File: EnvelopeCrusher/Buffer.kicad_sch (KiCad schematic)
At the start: 6 parts, among them U1 TL072

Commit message: Add routing
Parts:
- added C?: ~, symbol Device:C
- C? (x4): value 100nF -> ~; footprint Capacitor_SMD:C_0805_2012Metric_Pad1.18x1.45mm_HandSolder -> (none)
- R?: value 22M -> ~
- U1: value TL072 -> ~
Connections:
- net GND: now also C?.2
- net OUT: now also U1.6 (-), U1.7; no longer U1.1, U1.2 (-)
- net CRUSH_Z: now reaches U1.5 (+)
- net IN renamed DIRECT_OUT
- new net CRUSH_Y: U1.1, U1.2 (-)
- no-connect marks 3 -> 0
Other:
- note added: "74HC4066 Analog Switch"
- moved on the sheet: C?, R?, U1A, U1B

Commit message: updated
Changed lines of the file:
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@@
       (effects (font (size 1.27 1.27)) hide)
     )
-    (property "Value" "" (id 1) (at 130.81 125.0879 0))
+    (property "Value" "-5V" (id 1) (at 130.81 125.0879 0))
     (property "Footprint" "" (id 2) (at 130.81 130.1679 0)
       (effects (font (size 1.27 1.27)) hide)
@@
       (effects (font (size 1.27 1.27)) hide)
     )
-    (property "Value" "" (id 1) (at 143.51 161.29 0))
+    (property "Value" "GND" (id 1) (at 143.51 161.29 0))
     (property "Footprint" "" (id 2) (at 143.51 156.21 0)
       (effects (font (size 1.27 1.27)) hide)
@@
       (effects (font (size 1.27 1.27)) hide)
     )
-    (property "Value" "" (id 1) (at 58.42 97.79 0))
+    (property "Value" "GND" (id 1) (at 58.42 97.79 0))
     (property "Footprint" "" (id 2) (at 58.42 92.71 0)
       (effects (font (size 1.27 1.27)) hide)
@@
       (effects (font (size 1.27 1.27)) hide)
     )
-    (property "Value" "" (id 1) (at 177.165 106.68 0))
+    (property "Value" "GND" (id 1) (at 177.165 106.68 0))
     (property "Footprint" "" (id 2) (at 177.165 102.235 0)
       (effects (font (size 1.27 1.27)) hide)
@@
       (effects (font (size 1.27 1.27)) hide)
     )
-    (property "Value" "" (id 1) (at 67.31 125.0879 0))
+    (property "Value" "+5V" (id 1) (at 67.31 125.0879 0))
     (property "Footprint" "" (id 2) (at 67.31 130.1679 0)
       (effects (font (size 1.27 1.27)) hide)
@@
       (effects (font (size 1.27 1.27)) hide)
     )
-    (property "Value" "" (id 1) (at 54.61 161.29 0))
+    (property "Value" "GND" (id 1) (at 54.61 161.29 0))
     (property "Footprint" "" (id 2) (at 54.61 156.21 0)
       (effects (font (size 1.27 1.27)) hide)

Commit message: Completed Schematic
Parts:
- removed C?: ~, symbol Device:C
- removed R?: ~, symbol Device:R
- C15, C18: renamed from C?; value ~ -> 1uF
- C17: renamed from C?; value ~ -> 1uF; footprint (none) -> Capacitor_SMD:C_0805_2012Metric_Pad1.18x1.45mm_HandSolder
- gave numbers to parts that had none: 1
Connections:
- net CRUSH_Z: now also C19.1
- net IN: now reaches U1.3 (+)
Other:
- moved on the sheet: C19, U1A

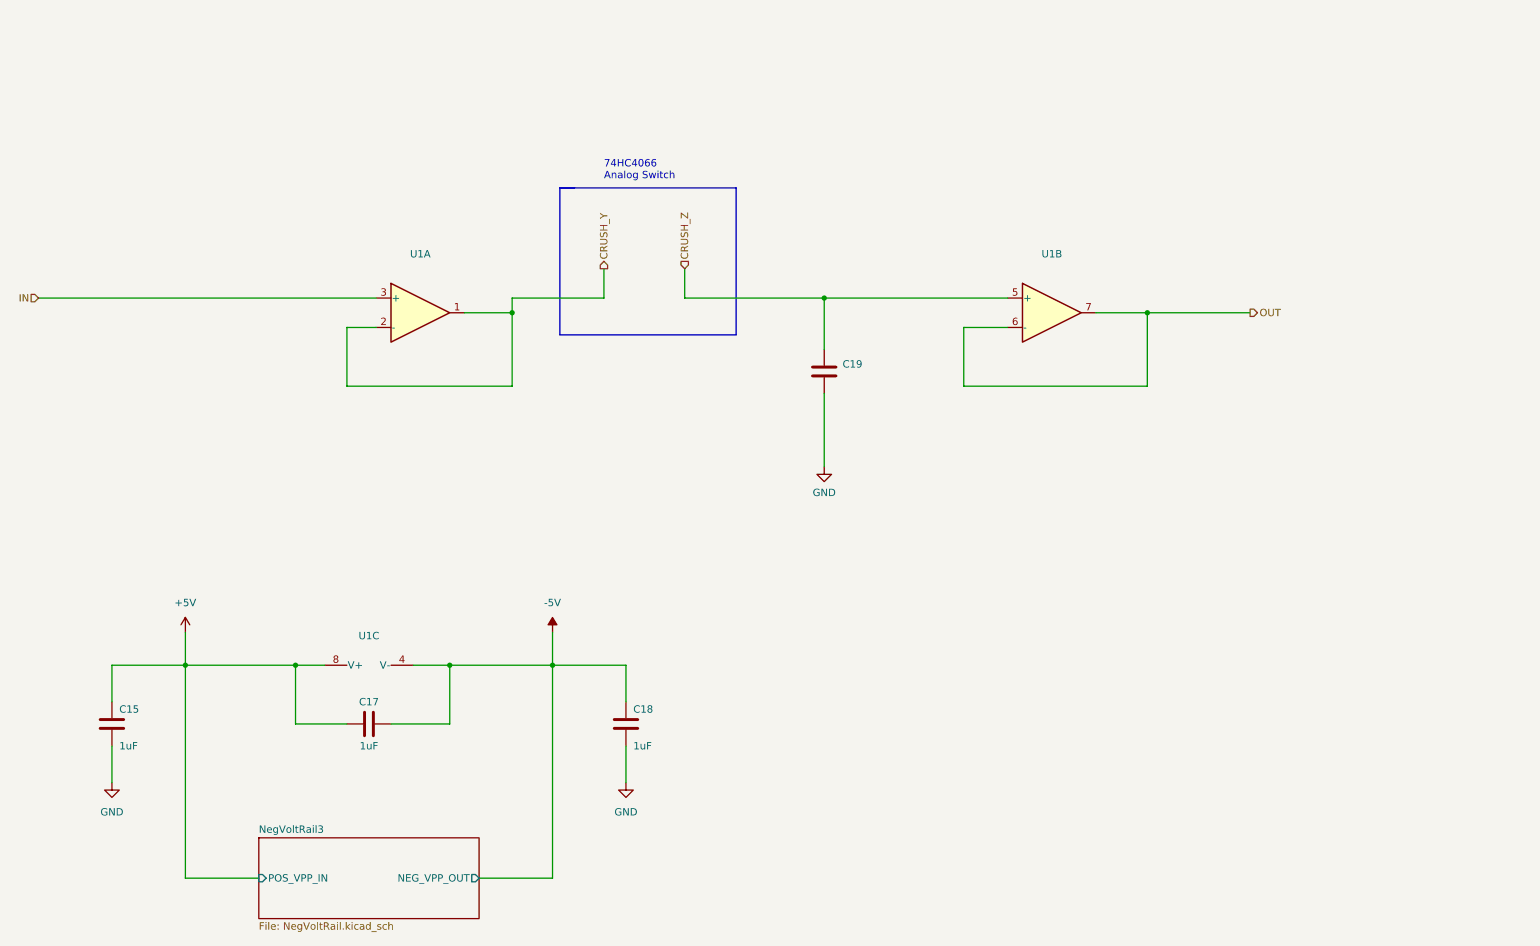
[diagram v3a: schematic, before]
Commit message: updated schematic
- Added values and comments to state-variable filter block
- Updated footprints
- Changed Dual Op Amp: TL072 to AM358
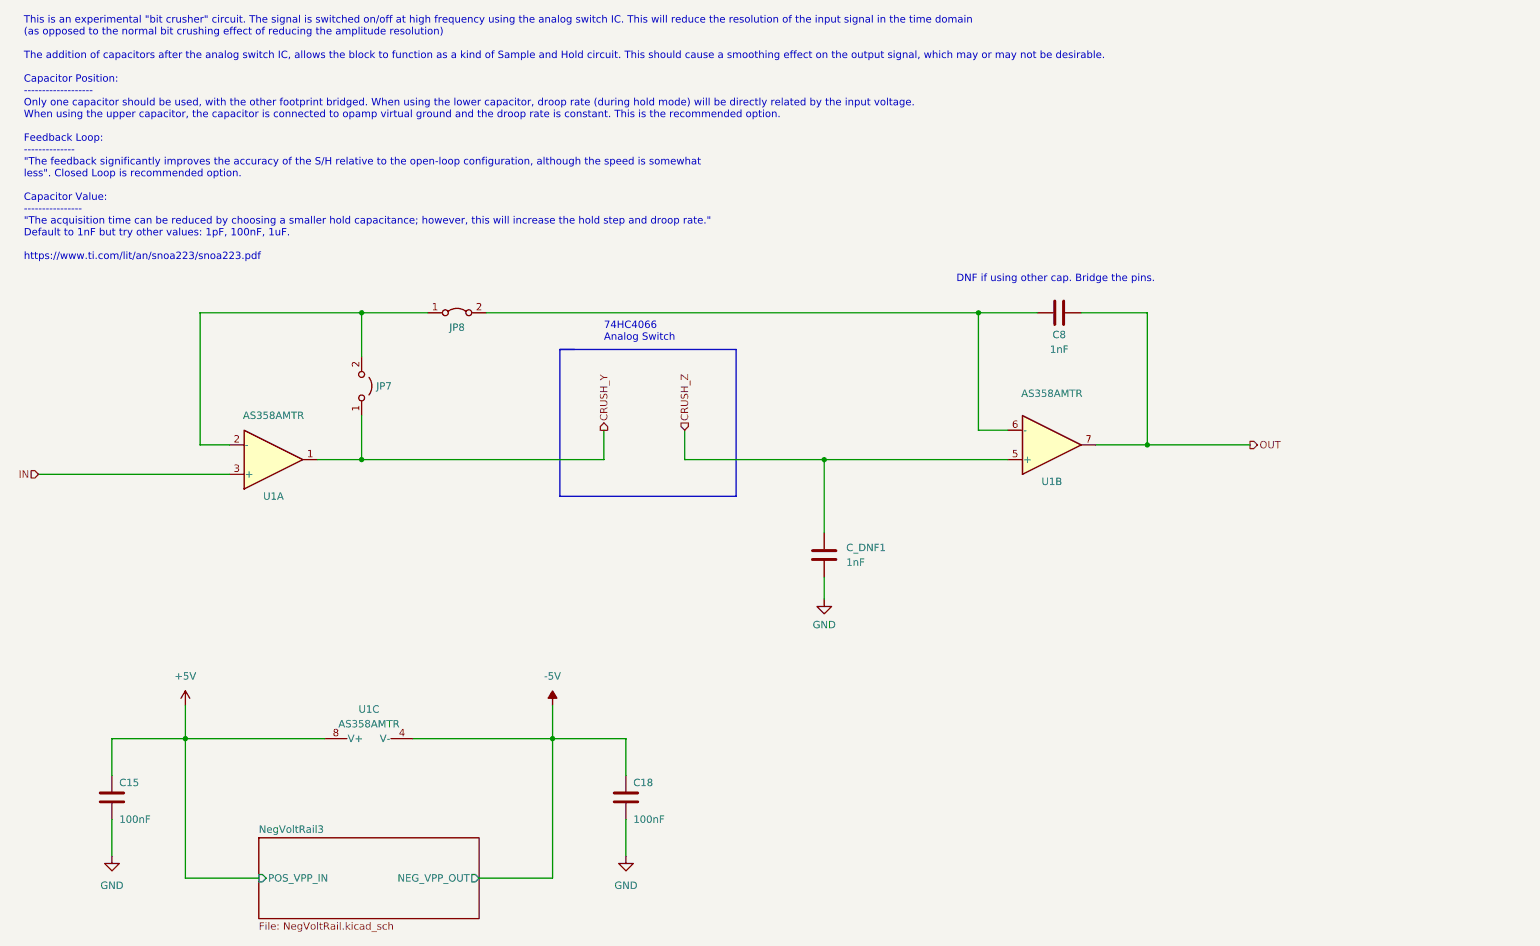
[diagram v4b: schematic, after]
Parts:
- removed C17: 1uF, Capacitor_SMD:C_0805_2012Metric_Pad1.18x1.45mm_HandSolder, symbol Device:C
- added C8: 1nF, Capacitor_SMD:C_0805_2012Metric_Pad1.18x1.45mm_HandSolder, symbol Device:C
- added JP7: Jumper_2_Open, Jumper:SolderJumper-2_P1.3mm_Open_Pad1.0x1.5mm, symbol Jumper:Jumper_2_Open
- added JP8: Jumper_2_Bridged, Jumper:SolderJumper-2_P1.3mm_Bridged_Pad1.0x1.5mm, symbol Jumper:Jumper_2_Bridged
- C15, C18: value 1uF -> 100nF; footprint (none) -> Capacitor_SMD:C_0805_2012Metric_Pad1.18x1.45mm_HandSolder
- C_DNF1: renamed from C19; value ~ -> 1nF; footprint (none) -> Capacitor_SMD:C_0805_2012Metric_Pad1.18x1.45mm_HandSolder
- U1: value ~ -> AS358AMTR; footprint (none) -> Package_SO:SOIC-8_3.9x4.9mm_P1.27mm
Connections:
- net CRUSH_Y: now also JP7.1 (A); no longer U1.2 (-)
- net OUT: now also C8.2; no longer U1.6 (-)
- new net: JP7.2 (B), JP8.1 (A), U1.2 (-)
- new net: C8.1, JP8.2 (B), U1.6 (-)
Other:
- note added: "DNF if using other cap. Bridge the pins."
- note added: "This is an experimental "bit crusher" circuit. The signal is switched on/off at high frequency using the analog switch IC. This will reduce the resolution of the input signal in the time domain (as opposed to the normal bit crushing effect of reducing the amplitude resolution) The addition of capacitors after the analog switch IC, allows the block to function as a kind of Sample and Hold circuit.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"
- moved on the sheet: C15, C18, C_DNF1, U1A, U1B, U1C

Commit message: organised layout into functional blocks
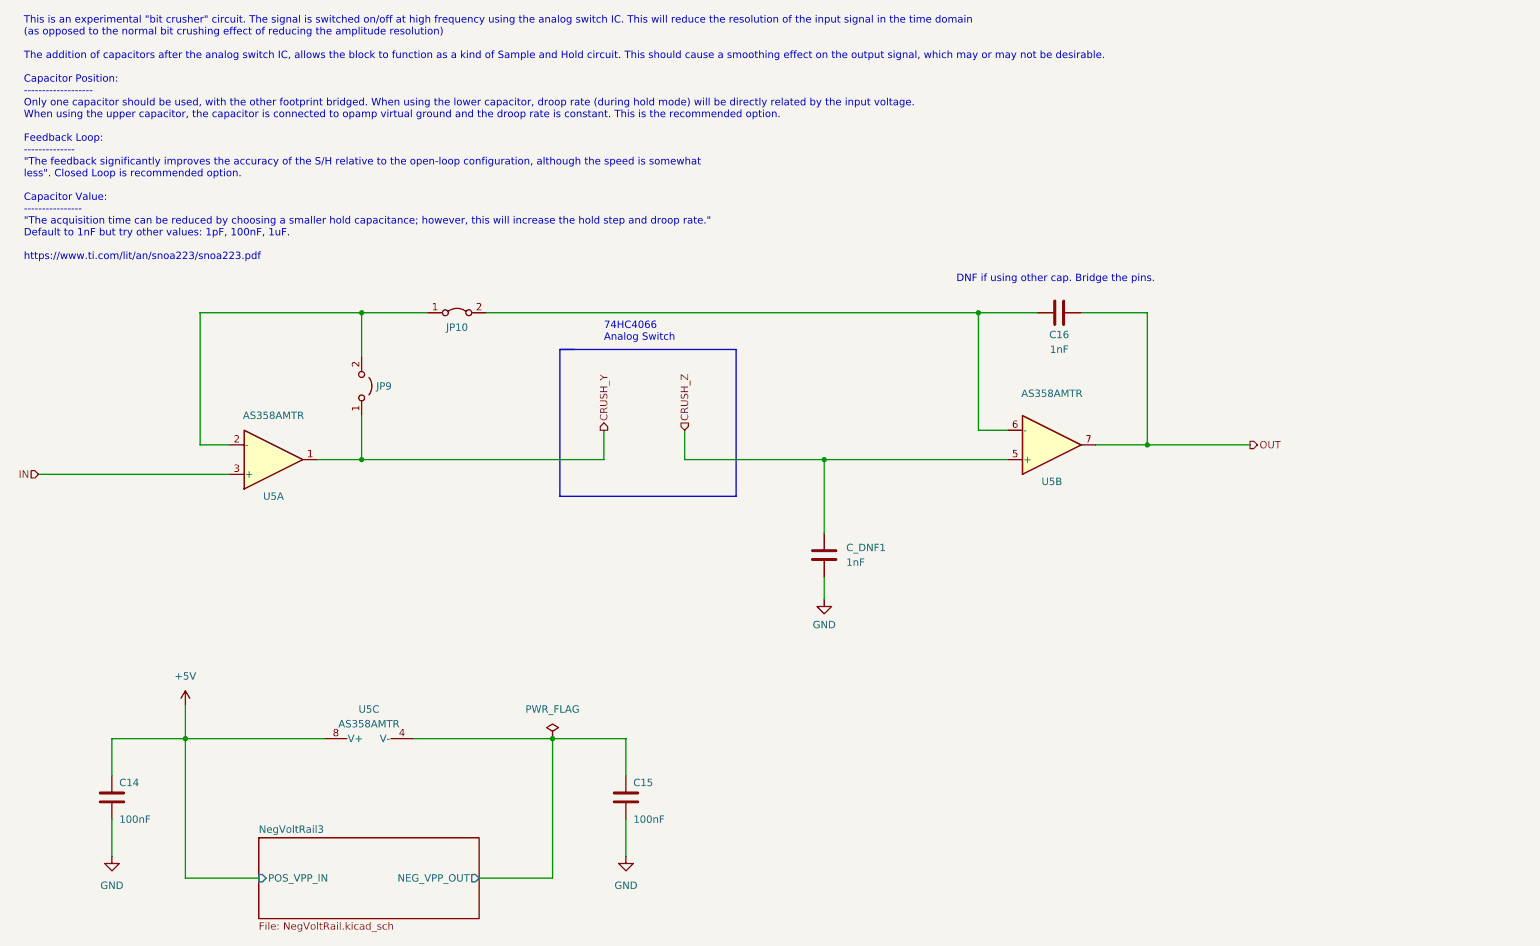
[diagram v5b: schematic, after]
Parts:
- renumbered C15 to C14, C18 to C15, C8 to C16, JP8 to JP10, JP7 to JP9, U1 to U5
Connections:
- net -5V renamed NegVoltRail3/NEG_VPP_OUT
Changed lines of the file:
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@@
-    (stroke (width 0) (type default) (color 0 0 0 0))
-  )
-  (wire (pts (xy 130.81 142.8679) (xy 130.81 148.59))
     (stroke (width 0) (type default) (color 0 0 0 0))
   )
@@
   (symbol (lib_id "Jumper:Jumper_2_Bridged") (at 114.3 74.93 0) (unit 1)
     (in_bom yes) (on_board yes)
-    (property "Reference" "JP8" (id 0) (at 114.3 77.47 0))
+    (property "Reference" "JP10" (id 0) (at 114.3 77.47 0))
     (property "Value" "Jumper_2_Bridged" (id 1) (at 114.3 71.12 0)
       (effects (font (size 1.27 1.27)) hide)
@@
     (pin "2")
   )
-  (symbol (lib_id "power:-5V") (at 130.81 142.8679 0) (unit 1)
-    (in_bom yes) (on_board yes) (fields_autoplaced)
-    (property "Reference" "#PWR034" (id 0) (at 130.81 140.3279 0)
-      (effects (font (size 1.27 1.27)) hide)
-    )
-    (property "Value" "-5V" (id 1) (at 130.81 137.7879 0))
-    (property "Footprint" "" (id 2) (at 130.81 142.8679 0)
-      (effects (font (size 1.27 1.27)) hide)
-    )
-    (property "Datasheet" "" (id 3) (at 130.81 142.8679 0)
-      (effects (font (size 1.27 1.27)) hide)
-    )
-    (pin "1")
-  )
   (symbol (lib_id "Jumper:Jumper_2_Open") (at 97.79 87.63 270) (mirror x) (unit 1)
     (in_bom yes) (on_board yes) (fields_autoplaced)
-    (property "Reference" "JP7" (id 0) (at 100.33 87.6299 90)
+    (property "Reference" "JP9" (id 0) (at 100.33 87.6299 90)
       (effects (font (size 1.27 1.27)) (justify left))
     )
@@
     (pin "1")
   )
+  (symbol (lib_id "power:PWR_FLAG") (at 130.81 148.59 0) (unit 1)
+    (in_bom yes) (on_board yes) (fields_autoplaced)
+    (property "Reference" "#FLG04" (id 0) (at 130.81 146.685 0)
+      (effects (font (size 1.27 1.27)) hide)
+    )
+    (property "Value" "PWR_FLAG" (id 1) (at 130.81 143.51 0))
+    (property "Footprint" "" (id 2) (at 130.81 148.59 0)
+      (effects (font (size 1.27 1.27)) hide)
+    )
+    (property "Datasheet" "~" (id 3) (at 130.81 148.59 0)
+      (effects (font (size 1.27 1.27)) hide)
+    )
+    (pin "1")
+  )
   (symbol (lib_id "Device:C") (at 218.44 74.93 90) (unit 1)
     (in_bom yes) (on_board yes)
-    (property "Reference" "C8" (id 0) (at 218.44 78.74 90))
+    (property "Reference" "C16" (id 0) (at 218.44 78.74 90))
     (property "Value" "1nF" (id 1) (at 218.44 81.28 90))
     (property "Footprint" "Capacitor_SMD:C_0805_2012Metric_Pad1.18x1.45mm_HandSolder" (id 2) (at 222.25 73.9648 0)
@@
   (symbol (lib_id "Amplifier_Operational:TL072") (at 217.17 97.79 0) (mirror x) (unit 2)
     (in_bom yes) (on_board yes)
-    (property "Reference" "U1" (id 0) (at 217.17 104.14 0))
+    (property "Reference" "U5" (id 0) (at 217.17 104.14 0))
     (property "Value" "AS358AMTR" (id 1) (at 217.17 88.9 0))
     (property "Footprint" "Package_SO:SOIC-8_3.9x4.9mm_P1.27mm" (id 2) (at 217.17 97.79 0)
@@
   (symbol (lib_id "power:+5V") (at 67.31 142.8679 0) (unit 1)
     (in_bom yes) (on_board yes) (fields_autoplaced)
-    (property "Reference" "#PWR033" (id 0) (at 67.31 146.6779 0)
+    (property "Reference" "#PWR034" (id 0) (at 67.31 146.6779 0)
       (effects (font (size 1.27 1.27)) hide)
     )
@@
   (symbol (lib_id "Amplifier_Operational:TL072") (at 99.06 146.05 90) (unit 3)
     (in_bom yes) (on_board yes) (fields_autoplaced)
-    (property "Reference" "U1" (id 0) (at 99.06 143.51 90))
+    (property "Reference" "U5" (id 0) (at 99.06 143.51 90))
     (property "Value" "AS358AMTR" (id 1) (at 99.06 146.05 90))
     (property "Footprint" "Package_SO:SOIC-8_3.9x4.9mm_P1.27mm" (id 2) (at 99.06 146.05 0)
@@
   (symbol (lib_id "Device:C") (at 143.51 158.75 180) (unit 1)
     (in_bom yes) (on_board yes)
-    (property "Reference" "C18" (id 0) (at 144.78 156.21 0)
+    (property "Reference" "C15" (id 0) (at 144.78 156.21 0)
       (effects (font (size 1.27 1.27)) (justify right))
     )
@@
   (symbol (lib_id "Device:C") (at 54.61 158.75 180) (unit 1)
     (in_bom yes) (on_board yes)
-    (property "Reference" "C15" (id 0) (at 55.88 156.21 0)
+    (property "Reference" "C14" (id 0) (at 55.88 156.21 0)
       (effects (font (size 1.27 1.27)) (justify right))
     )
@@
   (symbol (lib_id "power:GND") (at 54.61 168.91 0) (unit 1)
     (in_bom yes) (on_board yes) (fields_autoplaced)
-    (property "Reference" "#PWR031" (id 0) (at 54.61 175.26 0)
+    (property "Reference" "#PWR033" (id 0) (at 54.61 175.26 0)
       (effects (font (size 1.27 1.27)) hide)
     )
@@
   (symbol (lib_id "Amplifier_Operational:TL072") (at 82.55 100.33 0) (mirror x) (unit 1)
     (in_bom yes) (on_board yes)
-    (property "Reference" "U1" (id 0) (at 82.55 106.68 0))
+    (property "Reference" "U5" (id 0) (at 82.55 106.68 0))
     (property "Value" "AS358AMTR" (id 1) (at 82.55 92.71 0))
     (property "Footprint" "Package_SO:SOIC-8_3.9x4.9mm_P1.27mm" (id 2) (at 82.55 100.33 0)
